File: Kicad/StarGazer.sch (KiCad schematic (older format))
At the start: 12 parts, among them U101 STM32G070KBT6

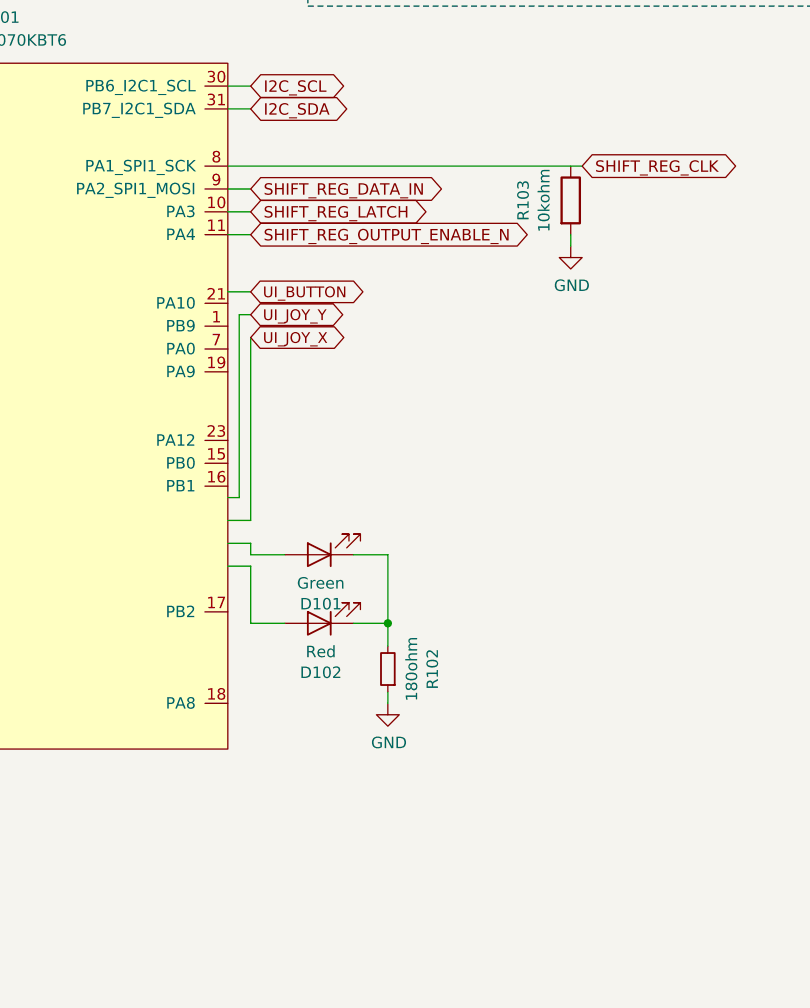
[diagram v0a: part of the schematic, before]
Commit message: PCB is likely complete.  Added USART for GPS.  Added background art and front label. Some leftover things are needed for the case.
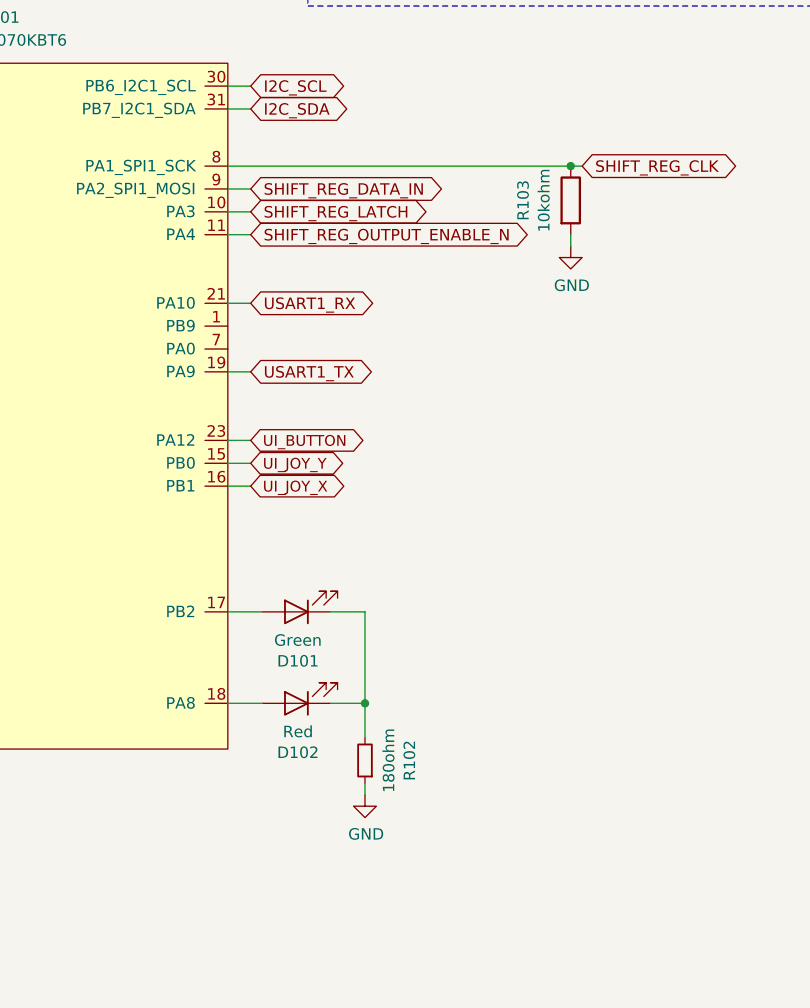
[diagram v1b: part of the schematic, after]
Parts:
- H101, H102, H103, H104: footprint MountingHole:MountingHole_2.2mm_M2 -> MountingHole:MountingHole_3.2mm_M3
- U101: part_name Cortex M0+ -> ARM Cortex M0+
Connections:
- net labels added: USART1_RX, USART1_TX
- wire segments 45 -> 41
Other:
- moved on the sheet: D101, D102, R102
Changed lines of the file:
@@
 Text GLabel 6700 3300 2    50   BiDi ~ 0
 SHIFT_REG_DATA_IN
-Text GLabel 6700 3750 2    47   BiDi ~ 0
+Text GLabel 6700 4400 2    47   BiDi ~ 0
 UI_BUTTON
-Text GLabel 6700 3950 2    47   BiDi ~ 0
+Text GLabel 6700 4600 2    47   BiDi ~ 0
 UI_JOY_X
-Text GLabel 6700 3850 2    47   BiDi ~ 0
+Text GLabel 6700 4500 2    47   BiDi ~ 0
 UI_JOY_Y
 $Sheet
@@
 F 3 "" H 5600 2600 50  0001 C CNN
 F 4 "64Mhz        Flash=128Kb, SRAM=32Kb" H 5600 2600 50  0001 C CNN "part_details"
-F 5 "Cortex M0+" H 5600 2600 50  0001 C CNN "part_name"
+F 5 "ARM Cortex M0+" H 5600 2600 50  0001 C CNN "part_name"
 F 6 "https://www.digikey.com/product-detail/en/stmicroelectronics/STM32G070KBT6/497-STM32G070KBT6-ND/10326752" H 5600 2600 50  0001 C CNN "part_url"
 	1    5600 2600
 	1    0    0    -1
 $EndComp
-Wire Wire Line
-	6700 3750 6600 3750
 Wire Wire Line
 	6700 3300 6600 3300
@@
 Wire Notes Line
 	6950 2500 10200 2500
-Wire Wire Line
-	6600 4650 6650 4650
-Wire Wire Line
-	6600 4750 6700 4750
 $Comp
 L Device:R_Small R102
 U 1 1 5F78816D
-P 7300 5400
+P 7200 5800
 AR Path="/5F78816D" Ref="R102"  Part="1"
 AR Path="/5F580D08/5F78816D" Ref="R?"  Part="1"
-F 0 "R102" V 7104 5400 50  0000 C CNN
-F 1 "180ohm" V 7195 5400 50  0000 C CNN
-F 2 "Resistor_SMD:R_1206_3216Metric_Pad1.42x1.75mm_HandSolder" H 7300 5400 50  0001 C CNN
-F 3 "~" H 7300 5400 50  0001 C CNN
-F 4 "Resistor - LED Status" H 7300 5400 50  0001 C CNN "part_name"
-F 5 "https://www.digikey.com/product-detail/en/stackpole-electronics-inc/RNCP1206FTD180R/RNCP1206FTD180RCT-ND/2240658" H 7300 5400 50  0001 C CNN "part_url"
-	1    7300 5400
+F 0 "R102" V 7004 5800 50  0000 C CNN
+F 1 "180ohm" V 7095 5800 50  0000 C CNN
+F 2 "Resistor_SMD:R_1206_3216Metric_Pad1.42x1.75mm_HandSolder" H 7200 5800 50  0001 C CNN
+F 3 "~" H 7200 5800 50  0001 C CNN
+F 4 "Resistor - LED Status" H 7200 5800 50  0001 C CNN "part_name"
+F 5 "https://www.digikey.com/product-detail/en/stackpole-electronics-inc/RNCP1206FTD180R/RNCP1206FTD180RCT-ND/2240658" H 7200 5800 50  0001 C CNN "part_url"
+	1    7200 5800
 	-1   0    0    1
 $EndComp
@@
 L Device:LED D102
 U 1 1 5F788176
-P 7000 5200
+P 6900 5550
 AR Path="/5F788176" Ref="D102"  Part="1"
 AR Path="/5F580D08/5F788176" Ref="D?"  Part="1"
-F 0 "D102" H 6993 5416 50  0000 C CNN
-F 1 "Red" H 6993 5325 50  0000 C CNN
-F 2 "Diode_SMD:D_1206_3216Metric" H 7000 5200 50  0001 C CNN
-F 3 "~" H 7000 5200 50  0001 C CNN
-F 4 "Debug Light" H 7000 5200 50  0001 C CNN "part_details"
-F 5 "https://www.digikey.com/product-detail/en/w%C3%BCrth-elektronik/156120RS75000/732-5030-1-ND/4490054" H 7000 5200 50  0001 C CNN "part_url"
-F 6 "LED - Red" H 7000 5200 50  0001 C CNN "part_name"
-	1    7000 5200
+F 0 "D102" H 6893 5766 50  0000 C CNN
+F 1 "Red" H 6893 5675 50  0000 C CNN
+F 2 "Diode_SMD:D_1206_3216Metric" H 6900 5550 50  0001 C CNN
+F 3 "~" H 6900 5550 50  0001 C CNN
+F 4 "Debug Light" H 6900 5550 50  0001 C CNN "part_details"
+F 5 "https://www.digikey.com/product-detail/en/w%C3%BCrth-elektronik/156120RS75000/732-5030-1-ND/4490054" H 6900 5550 50  0001 C CNN "part_url"
+F 6 "LED - Red" H 6900 5550 50  0001 C CNN "part_name"
+	1    6900 5550
 	-1   0    0    1
 $EndComp
@@
 L Device:LED D101
 U 1 1 5F78817F
-P 7000 4900
+P 6900 5150
 AR Path="/5F78817F" Ref="D101"  Part="1"
 AR Path="/5F580D08/5F78817F" Ref="D?"  Part="1"
-F 0 "D101" H 6993 5116 50  0000 C CNN
-F 1 "Green" H 6993 5025 50  0000 C CNN
-F 2 "Diode_SMD:D_1206_3216Metric" H 7000 4900 50  0001 C CNN
-F 3 "~" H 7000 4900 50  0001 C CNN
-F 4 "Debug Light" H 7000 4900 50  0001 C CNN "part_details"
-F 5 "LED - Green" H 7000 4900 50  0001 C CNN "part_name"
-F 6 "https://www.digikey.com/product-detail/en/w%C3%BCrth-elektronik/156120VS75000/732-5032-1-ND/4490060" H 7000 4900 50  0001 C CNN "part_url"
-	1    7000 4900
+F 0 "D101" H 6893 5366 50  0000 C CNN
+F 1 "Green" H 6893 5275 50  0000 C CNN
+F 2 "Diode_SMD:D_1206_3216Metric" H 6900 5150 50  0001 C CNN
+F 3 "~" H 6900 5150 50  0001 C CNN
+F 4 "Debug Light" H 6900 5150 50  0001 C CNN "part_details"
+F 5 "LED - Green" H 6900 5150 50  0001 C CNN "part_name"
+F 6 "https://www.digikey.com/product-detail/en/w%C3%BCrth-elektronik/156120VS75000/732-5032-1-ND/4490060" H 6900 5150 50  0001 C CNN "part_url"
+	1    6900 5150
 	-1   0    0    1
 $EndComp
-Wire Wire Line
-	6700 4950 6600 4950
-Wire Wire Line
-	6700 4950 6700 5200
-Wire Wire Line
-	6700 5200 6850 5200
-Wire Wire Line
-	6600 4850 6700 4850
-Wire Wire Line
-	6700 4850 6700 4900
-Wire Wire Line
-	6700 4900 6850 4900
 $Comp
 L power:GND #PWR0103
 U 1 1 5F79138F
-P 7300 5550
-F 0 "#PWR0103" H 7300 5300 50  0001 C CNN
-F 1 "GND" H 7305 5377 50  0000 C CNN
-F 2 "" H 7300 5550 50  0001 C CNN
-F 3 "" H 7300 5550 50  0001 C CNN
-	1    7300 5550
+P 7200 5950
+F 0 "#PWR0103" H 7200 5700 50  0001 C CNN
+F 1 "GND" H 7205 5777 50  0000 C CNN
+F 2 "" H 7200 5950 50  0001 C CNN
+F 3 "" H 7200 5950 50  0001 C CNN
+	1    7200 5950
 	1    0    0    -1
 $EndComp
@@
 F 0 "H103" H 4900 7246 50  0000 L CNN
 F 1 "MountingHole" H 4900 7155 50  0000 L CNN
-F 2 "MountingHole:MountingHole_2.2mm_M2" H 4800 7200 50  0001 C CNN
+F 2 "MountingHole:MountingHole_3.2mm_M3" H 4800 7200 50  0001 C CNN
 F 3 "~" H 4800 7200 50  0001 C CNN
 F 4 "DO_NOT_SHOW" H 4800 7200 50  0001 C CNN "part_details"
@@
 F 0 "H104" H 4900 7446 50  0000 L CNN
 F 1 "MountingHole" H 4900 7355 50  0000 L CNN
-F 2 "MountingHole:MountingHole_2.2mm_M2" H 4800 7400 50  0001 C CNN
+F 2 "MountingHole:MountingHole_3.2mm_M3" H 4800 7400 50  0001 C CNN
 F 3 "~" H 4800 7400 50  0001 C CNN
 F 4 "DO_NOT_SHOW" H 4800 7400 50  0001 C CNN "part_details"
@@
 F 0 "H101" H 4900 6796 50  0000 L CNN
 F 1 "MountingHole" H 4900 6705 50  0000 L CNN
-F 2 "MountingHole:MountingHole_2.2mm_M2" H 4800 6750 50  0001 C CNN
+F 2 "MountingHole:MountingHole_3.2mm_M3" H 4800 6750 50  0001 C CNN
 F 3 "~" H 4800 6750 50  0001 C CNN
 F 4 "DO_NOT_SHOW" H 4800 6750 50  0001 C CNN "part_details"
@@
 F 0 "H102" H 4900 6996 50  0000 L CNN
 F 1 "MountingHole" H 4900 6905 50  0000 L CNN
-F 2 "MountingHole:MountingHole_2.2mm_M2" H 4800 6950 50  0001 C CNN
+F 2 "MountingHole:MountingHole_3.2mm_M3" H 4800 6950 50  0001 C CNN
 F 3 "~" H 4800 6950 50  0001 C CNN
 F 4 "DO_NOT_SHOW" H 4800 6950 50  0001 C CNN "part_details"
@@
 $EndComp
 Wire Wire Line
-	7150 5200 7300 5200
-Wire Wire Line
-	7300 5200 7300 5300
-Wire Wire Line
-	7150 4900 7300 4900
-Wire Wire Line
-	7300 4900 7300 5200
-Connection ~ 7300 5200
-Wire Wire Line
-	7300 5550 7300 5500
-Wire Wire Line
-	6650 4650 6650 3850
-Wire Wire Line
-	6650 3850 6700 3850
-Wire Wire Line
-	6700 3950 6700 4750
-Wire Wire Line
-	6600 3200 8150 3200
+	7050 5550 7200 5550
+Wire Wire Line
+	7200 5550 7200 5700
+Wire Wire Line
+	7050 5150 7200 5150
+Wire Wire Line
+	7200 5150 7200 5550
+Connection ~ 7200 5550
+Wire Wire Line
+	7200 5950 7200 5900
 Wire Wire Line
 	8100 3550 8100 3500
@@
 	1    0    0    -1
 $EndComp
+Wire Wire Line
+	6600 3200 8100 3200
+Connection ~ 8100 3200
+Wire Wire Line
+	8100 3200 8150 3200
+Text GLabel 6700 3800 2    50   BiDi ~ 0
+USART1_RX
+Wire Wire Line
+	6600 5550 6750 5550
+Wire Wire Line
+	6600 5150 6750 5150
+Wire Wire Line
+	6600 3800 6700 3800
+Wire Wire Line
+	6700 4500 6600 4500
+Wire Wire Line
+	6600 4600 6700 4600
+Wire Wire Line
+	6600 4400 6700 4400
+Wire Wire Line
+	6600 4100 6700 4100
+Text GLabel 6700 4100 2    50   BiDi ~ 0
+USART1_TX
 $EndSCHEMATC

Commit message: Purchases made, case ordered, PCB ordered, parts ordered, money not happy.
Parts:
- C101, C102, D101, D102: PURCHASED (none) -> 6x
- H101, H102, H103, H104: PURCHASED (none) -> x
- R101, R103: PURCHASED (none) -> 24x
- R102: PURCHASED (none) -> 9x
- U101: PURCHASED (none) -> 3x
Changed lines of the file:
@@
 F 5 "ARM Cortex M0+" H 5600 2600 50  0001 C CNN "part_name"
 F 6 "https://www.digikey.com/product-detail/en/stmicroelectronics/STM32G070KBT6/497-STM32G070KBT6-ND/10326752" H 5600 2600 50  0001 C CNN "part_url"
+F 7 "3x" H 5600 2600 50  0001 C CNN "PURCHASED"
 	1    5600 2600
 	1    0    0    -1
@@
 F 4 "https://www.digikey.com/product-detail/en/w%C3%BCrth-elektronik/885012107009/732-7619-1-ND/5454246" H 4200 2700 50  0001 C CNN "part_url"
 F 5 "Capactitor - Bypass" H 4200 2700 50  0001 C CNN "part_name"
+F 6 "6x" H 4200 2700 50  0001 C CNN "PURCHASED"
 	1    4200 2700
 	0    1    1    0
@@
 F 5 "https://www.digikey.com/product-detail/en/w%C3%BCrth-elektronik/885012107009/732-7619-1-ND/5454246" H 4200 2350 50  0001 C CNN "part_url"
 F 6 "Capactitor - Bypass" H 4200 2350 50  0001 C CNN "part_name"
+F 7 "6x" H 4200 2350 50  0001 C CNN "PURCHASED"
 	1    4200 2350
 	0    1    1    0
@@
 F 6 "Resistor - Pull Up" H 4000 3600 50  0001 C CNN "part_name"
 F 7 "https://www.digikey.com/product-detail/en/yageo/RC1206JR-0710KL/311-10KERCT-ND/732156" H 4000 3600 50  0001 C CNN "part_url"
+F 8 "24x" H 4000 3600 50  0001 C CNN "PURCHASED"
 	1    4000 3600
 	1    0    0    -1
@@
 F 4 "Resistor - LED Status" H 7200 5800 50  0001 C CNN "part_name"
 F 5 "https://www.digikey.com/product-detail/en/stackpole-electronics-inc/RNCP1206FTD180R/RNCP1206FTD180RCT-ND/2240658" H 7200 5800 50  0001 C CNN "part_url"
+F 6 "9x" H 7200 5800 50  0001 C CNN "PURCHASED"
 	1    7200 5800
 	-1   0    0    1
@@
 F 5 "https://www.digikey.com/product-detail/en/w%C3%BCrth-elektronik/156120RS75000/732-5030-1-ND/4490054" H 6900 5550 50  0001 C CNN "part_url"
 F 6 "LED - Red" H 6900 5550 50  0001 C CNN "part_name"
+F 7 "6x" H 6900 5550 50  0001 C CNN "PURCHASED"
 	1    6900 5550
 	-1   0    0    1
@@
 F 5 "LED - Green" H 6900 5150 50  0001 C CNN "part_name"
 F 6 "https://www.digikey.com/product-detail/en/w%C3%BCrth-elektronik/156120VS75000/732-5032-1-ND/4490060" H 6900 5150 50  0001 C CNN "part_url"
+F 7 "6x" H 6900 5150 50  0001 C CNN "PURCHASED"
 	1    6900 5150
 	-1   0    0    1
@@
 F 3 "~" H 4800 7200 50  0001 C CNN
 F 4 "DO_NOT_SHOW" H 4800 7200 50  0001 C CNN "part_details"
+F 5 "x" H 4800 7200 50  0001 C CNN "PURCHASED"
 	1    4800 7200
 	1    0    0    -1
@@
 F 3 "~" H 4800 7400 50  0001 C CNN
 F 4 "DO_NOT_SHOW" H 4800 7400 50  0001 C CNN "part_details"
+F 5 "x" H 4800 7400 50  0001 C CNN "PURCHASED"
 	1    4800 7400
 	1    0    0    -1
@@
 F 3 "~" H 4800 6750 50  0001 C CNN
 F 4 "DO_NOT_SHOW" H 4800 6750 50  0001 C CNN "part_details"
+F 5 "x" H 4800 6750 50  0001 C CNN "PURCHASED"
 	1    4800 6750
 	1    0    0    -1
@@
 F 3 "~" H 4800 6950 50  0001 C CNN
 F 4 "DO_NOT_SHOW" H 4800 6950 50  0001 C CNN "part_details"
+F 5 "x" H 4800 6950 50  0001 C CNN "PURCHASED"
 	1    4800 6950
 	1    0    0    -1
@@
 F 6 "Resistor - Pull Up" H 8100 3350 50  0001 C CNN "part_name"
 F 7 "https://www.digikey.com/product-detail/en/yageo/RC1206JR-0710KL/311-10KERCT-ND/732156" H 8100 3350 50  0001 C CNN "part_url"
+F 8 "24x" H 8100 3350 50  0001 C CNN "PURCHASED"
 	1    8100 3350
 	1    0    0    -1
